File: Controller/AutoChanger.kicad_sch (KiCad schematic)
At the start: 30 parts, among them J1 OLED, P10 SENSOR, P11 SENSOR, P12 LOGO, P3 1, P4 2, P5 3, P6 4, P8 M3, P9 M3, SW1 RESET, SW2 1, SW3 2, SW4 3, SW5 4, SW6 PRGM, U1 TinyPico, U2 PCA9685PW, U3 ITR9606-F

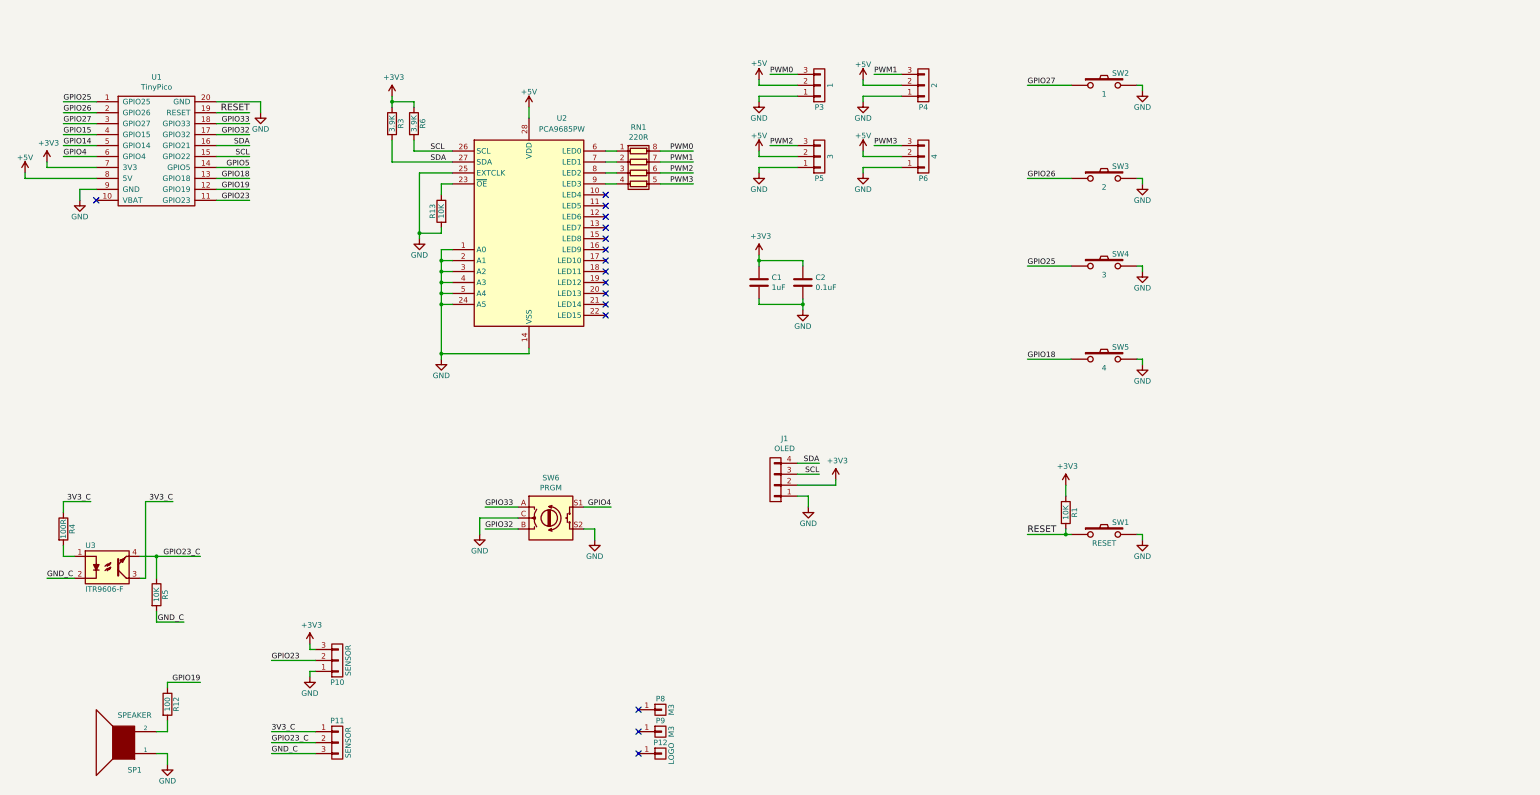
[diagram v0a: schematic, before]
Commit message: Circuit Board updated to version 3.0
Circuit board no longer uses a TinyPICO.  It uses a ESP32-S3-WROOM module instead.  It is also 90% SMD parts and can be assembled by JLCPCB
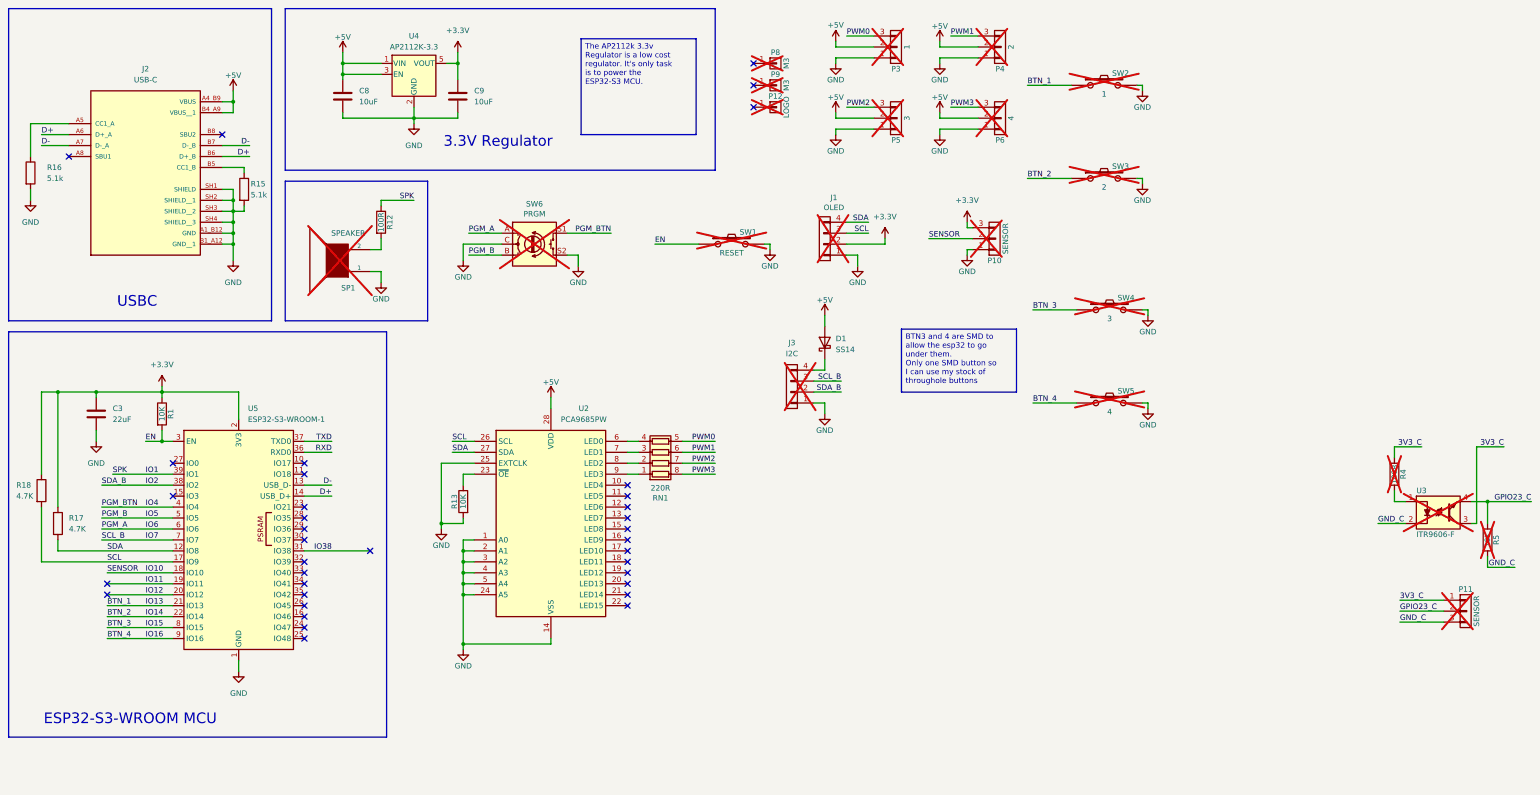
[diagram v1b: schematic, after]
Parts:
- removed C1: 1uF, Capacitor_SMD:C_0603_1608Metric_Pad1.05x0.95mm_HandSolder, symbol Device:C
- removed C2: 0.1uF, Capacitor_SMD:C_0603_1608Metric_Pad1.05x0.95mm_HandSolder, symbol Device:C
- removed R3, R6: 3.9K, Resistor_SMD:R_0603_1608Metric_Pad1.05x0.95mm_HandSolder, symbol Device:R
- removed U1: TinyPico, libs:TinyPico, symbol tinypico:TinyPico
- added C3: 22uF, Capacitor_SMD:C_0603_1608Metric, symbol Device:C
- added C8, C9: 10uF, Capacitor_SMD:C_0603_1608Metric, symbol Device:C
- added D1: SS14, Diode_SMD:D_SMA_Handsoldering, symbol Diode:SS14
- added J2: USB-C, libs:AMPHENOL_12402012E212A, symbol think2switch:12402012E212A
- added J3: I2C, Connector_PinHeader_2.54mm:PinHeader_1x04_P2.54mm_Vertical, symbol AutoChanger-rescue:CONN_01X04
- added R15, R16: 5.1k, Resistor_SMD:R_0603_1608Metric_Pad0.98x0.95mm_HandSolder, symbol Device:R
- added R17, R18: 4.7K, Resistor_SMD:R_0603_1608Metric_Pad0.98x0.95mm_HandSolder, symbol Device:R
- added U4: AP2112K-3.3, Package_TO_SOT_SMD:SOT-23-5, symbol Regulator_Linear:AP2112K-3.3
- added U5: ESP32-S3-WROOM-1, RF_Module:ESP32-S3-WROOM-1, symbol RF_Module:ESP32-S3-WROOM-1
- J1, P12, SW6, U3: now not fitted
- P10, P11, P3, P4, P5, P6: footprint Pin_Headers:Pin_Header_Straight_1x03_Pitch2.54mm -> Connector_PinHeader_2.54mm:PinHeader_1x03_P2.54mm_Vertical; now not fitted
- P8, P9: footprint Connect:1pin -> MountingHole:MountingHole_3.2mm_M3; now not fitted
- R1: footprint Resistors_SMD:R_0603_HandSoldering -> Resistor_SMD:R_0603_1608Metric_Pad0.98x0.95mm_HandSolder; LCSC (none) -> C25804
- R12: value 100 -> 100R; footprint Resistors_SMD:R_0603_HandSoldering -> Resistor_SMD:R_0603_1608Metric_Pad0.98x0.95mm_HandSolder; LCSC (none) -> C22775
- R13: footprint Resistor_SMD:R_0603_1608Metric_Pad1.05x0.95mm_HandSolder -> Resistor_SMD:R_0603_1608Metric_Pad0.98x0.95mm_HandSolder; LCSC (none) -> C25804
- R4: footprint Resistors_SMD:R_0603_HandSoldering -> Resistor_SMD:R_0603_1608Metric_Pad0.98x0.95mm_HandSolder; LCSC (none) -> C22775; now not fitted
- R5: footprint Resistors_SMD:R_0603_HandSoldering -> Resistor_SMD:R_0603_1608Metric_Pad0.98x0.95mm_HandSolder; LCSC (none) -> C25804; now not fitted
- RN1: LCSC (none) -> C29719
- SP1: footprint Buzzers_Beepers:Buzzer_12x9.5RM7.6 -> Buzzer_Beeper:Buzzer_12x9.5RM7.6; now not fitted
- SW1: footprint Buttons_Switches_ThroughHole:SW_PUSH_SMALL -> Button_Switch_THT:SW_PUSH_6mm; now not fitted
- SW2, SW3, SW4, SW5: footprint Buttons_Switches_ThroughHole:SW_PUSH_SMALL -> Button_Switch_SMD:SW_SPST_PTS645Sx43SMTR92; now not fitted
- U2: LCSC (none) -> C2678753
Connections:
- net +5V: now also C8.1, D1.2 (A), J2.A4_B9 (VBUS), J2.B4_A9 (VBUS__1), U4.1 (VIN), U4.3 (EN)
- net GND: now also C3.2, C8.2, C9.2, J2.A1_B12 (GND), J2.B1_A12 (GND__1), J2.SH1 (SHIELD), J2.SH2 (SHIELD__1), J2.SH3 (SHIELD__2), J2.SH4 (SHIELD__3), J3.1 (P1), R15.2, R16.2, U4.2 (GND), U5.1 (GND), U5.40 (GND), U5.41 (GND)
- net PWM0: now also RN1.5 (R4.2); no longer RN1.8 (R1.2)
- net PWM1: now also RN1.6 (R3.2); no longer RN1.7 (R2.2)
- net PWM2: now also RN1.7 (R2.2); no longer RN1.6 (R3.2)
- net PWM3: now also RN1.8 (R1.2); no longer RN1.5 (R4.2)
- net SCL: now also R18.2, U5.17 (IO9)
- net SDA: now also R17.2, U5.12 (IO8)
- net at U2.6 (LED0): now also RN1.4 (R4.1); no longer RN1.1 (R1.1)
- net at U2.7 (LED1): now also RN1.3 (R3.1); no longer RN1.2 (R2.1)
- net at U2.8 (LED2): now also RN1.2 (R2.1); no longer RN1.3 (R3.1)
- net at U2.9 (LED3): now also RN1.1 (R1.1); no longer RN1.4 (R4.1)
- net +3V3 renamed +3.3V
- net +3.3V: now also C3.1, C9.1, R17.1, R18.1, U4.5 (VOUT), U5.2 (3V3)
- net GPIO18 renamed BTN_4
- net BTN_4: now also U5.9 (IO16)
- net GPIO19 renamed IO1
- net IO1: now also U5.39 (IO1)
- net GPIO23 renamed IO10
- net IO10: now also U5.18 (IO10)
- net GPIO25 renamed BTN_3
- net BTN_3: now also U5.8 (IO15)
- net GPIO26 renamed BTN_2
- net BTN_2: now also U5.22 (IO14)
- net GPIO27 renamed BTN_1
- net BTN_1: now also U5.21 (IO13)
- net GPIO32 renamed IO5
- net IO5: now also U5.5 (IO5)
- net GPIO33 renamed IO6
- net IO6: now also U5.6 (IO6)
- net GPIO4 renamed IO4
- net IO4: now also U5.4 (IO4)
- net RESET renamed EN
- net EN: now also U5.3 (EN)
- new net: J2.A5 (CC1_A), R16.1
- new net: J2.B5 (CC1_B), R15.1
- new net: D1.1 (K), J3.4 (P4)
- new net D+: J2.A6 (D+_A), J2.B6 (D+_B), U5.14 (USB_D+)
- new net D-: J2.A7 (D-_A), J2.B7 (D-_B), U5.13 (USB_D-)
- new net IO11: U5.19 (IO11)
- new net IO12: U5.20 (IO12)
- new net IO2: J3.2 (P2), U5.38 (IO2)
- new net IO38: U5.31 (IO38)
- new net IO7: J3.3 (P3), U5.7 (IO7)
- new net RXD: U5.36 (RXD0)
- new net TXD: U5.37 (TXD0)
- no-connect marks 16 -> 36
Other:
- note added: "3.3V Regulator"
- note added: "ESP32-S3-WROOM MCU"
- note added: "USBC"
- moved on the sheet: R1, R12, R13, RN1, U2

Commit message: changes to jlcpcb tags
Improving jlcpcb manufacturability.  Ideally none of the parts are hand placed.
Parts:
- removed P3: 1, Connector_PinHeader_2.54mm:PinHeader_1x03_P2.54mm_Vertical, symbol AutoChanger-rescue:CONN_01X03
- removed P4: 2, Connector_PinHeader_2.54mm:PinHeader_1x03_P2.54mm_Vertical, symbol AutoChanger-rescue:CONN_01X03
- removed P5: 3, Connector_PinHeader_2.54mm:PinHeader_1x03_P2.54mm_Vertical, symbol AutoChanger-rescue:CONN_01X03
- removed P6: 4, Connector_PinHeader_2.54mm:PinHeader_1x03_P2.54mm_Vertical, symbol AutoChanger-rescue:CONN_01X03
- added J5: HX PZ2.54-4x3P, libs:HX PZ2.54-4x3P, symbol Connector_Generic:Conn_02x06_Odd_Even
- J1: LCSC (none) -> C5248081; now fitted
- J3: LCSC (none) -> C5224015; now fitted
- P10: LCSC (none) -> C32713262; now fitted
- SW1: footprint Button_Switch_THT:SW_PUSH_6mm -> Button_Switch_SMD:SW_SPST_PTS645Sx43SMTR92; LCSC (none) -> C557614; now fitted
- SW2, SW3, SW4, SW5: LCSC (none) -> C53202676; now fitted
- SW6: LCSC (none) -> C470742; now fitted
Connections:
- net +5V: now also J5.5 (Pin_5), J5.6 (Pin_6), J5.7 (Pin_7), J5.8 (Pin_8)
- net GND: now also J5.1 (Pin_1), J5.2 (Pin_2), J5.3 (Pin_3), J5.4 (Pin_4)
- net PWM0: now also J5.9 (Pin_9)
- net PWM1: now also J5.10 (Pin_10)
- net PWM2: now also J5.11 (Pin_11)
- net PWM3: now also J5.12 (Pin_12)

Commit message: Circuit board Version 3.1
Improvements made to allow manufacturing with PnP machines.
Geometry is largely unchanged.
i2c for connections to other systems now has level shifting.
the sensor and the i2c connector are now using PST 2.0 plugs rather than dupont.
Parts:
- removed J5: HX PZ2.54-4x3P, libs:HX PZ2.54-4x3P, symbol Connector_Generic:Conn_02x06_Odd_Even
- added J4: 03-04, libs:HDR-SMD_6P-P2.54-V-M-R2-C3-LS7.5-2, symbol Connector_Generic:Conn_02x03_Odd_Even
- added J6: 01-02, libs:HDR-SMD_6P-P2.54-V-M-R2-C3-LS7.5-2, symbol Connector_Generic:Conn_02x03_Odd_Even
- added Q1, Q2: BSS138, Package_TO_SOT_SMD:SOT-23, symbol Transistor_FET:BSS138
- added RN2: 10K, Resistor_SMD:R_Array_Convex_4x0603, symbol Device:R_Pack04_Split
- D1: footprint Diode_SMD:D_SMA_Handsoldering -> Diode_SMD:D_SMA
- J3: footprint Connector_PinHeader_2.54mm:PinHeader_1x04_P2.54mm_Vertical -> libs:CONN-SMD_PH2.0MM-4P-WT; LCSC C5224015 -> C53055420
- P10: footprint Connector_PinHeader_2.54mm:PinHeader_1x03_P2.54mm_Vertical -> libs:CONN-SMD_PH2.0MM-3P-WT; LCSC C32713262 -> C53055419
- SW6: now not fitted
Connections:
- net +3.3V: now also Q1.1 (G), Q2.1 (G), RN2.5 (R4.2), RN2.7 (R2.2)
- net +5V: now also J4.3 (Pin_3), J4.4 (Pin_4), J6.3 (Pin_3), J6.4 (Pin_4), RN2.6 (R3.2), RN2.8 (R1.2)
- net GND: now also J4.1 (Pin_1), J4.2 (Pin_2), J6.1 (Pin_1), J6.2 (Pin_2)
- net IO2: now also Q1.2 (S), RN2.2 (R2.1); no longer J3.2 (P2)
- net IO7: now also Q2.2 (S), RN2.4 (R4.1); no longer J3.3 (P3)
- net PWM0: now also J6.6 (Pin_6)
- net PWM1: now also J6.5 (Pin_5)
- net PWM2: now also J4.6 (Pin_6)
- net PWM3: now also J4.5 (Pin_5)
- new net SCL_B_5v: J3.3 (P3), Q2.3 (D), RN2.3 (R3.1)
- new net SDA_B_5V: J3.2 (P2), Q1.3 (D), RN2.1 (R1.1)
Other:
- moved on the sheet: SW2, SW3, SW4, SW5
